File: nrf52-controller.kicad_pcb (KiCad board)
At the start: 8 copper layers, 32.3 x 27.6 mm, 94 parts, among them J1 Conn_01x01_Pin, J2 Conn_01x01_Pin, J3 USB_C_Receptacle_USB2.0, J4 Conn_01x01_Pin, J5 Conn_01x01_Pin, J6 Conn_ARM_JTAG_SWD_10, J7 FH35C-41S-0.3SHW, SW1 434351045816, SW2 434351045816, U1 MAX17048G+T10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

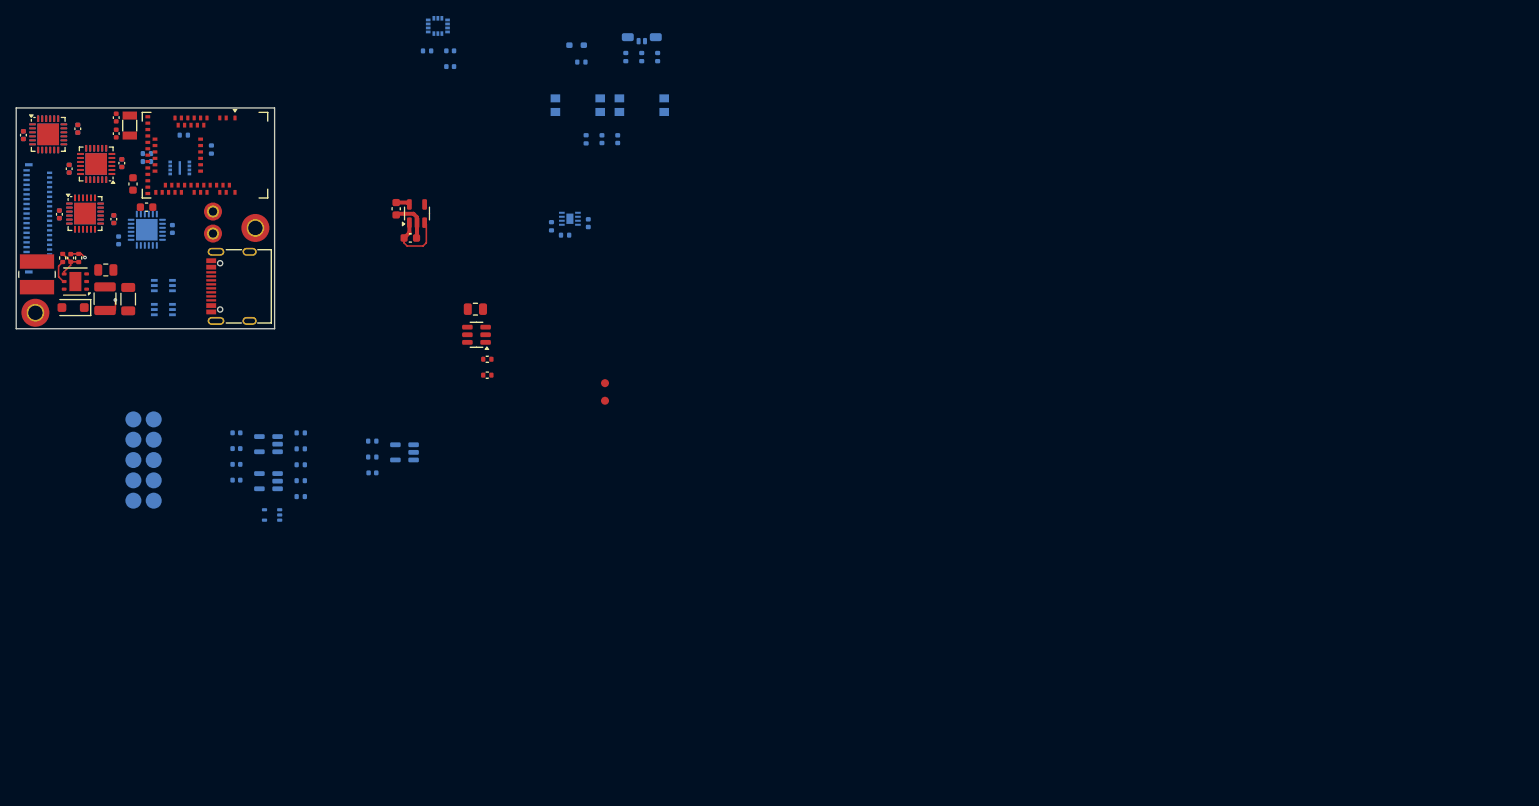
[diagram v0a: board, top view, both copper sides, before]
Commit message: separated smaller board layout variant
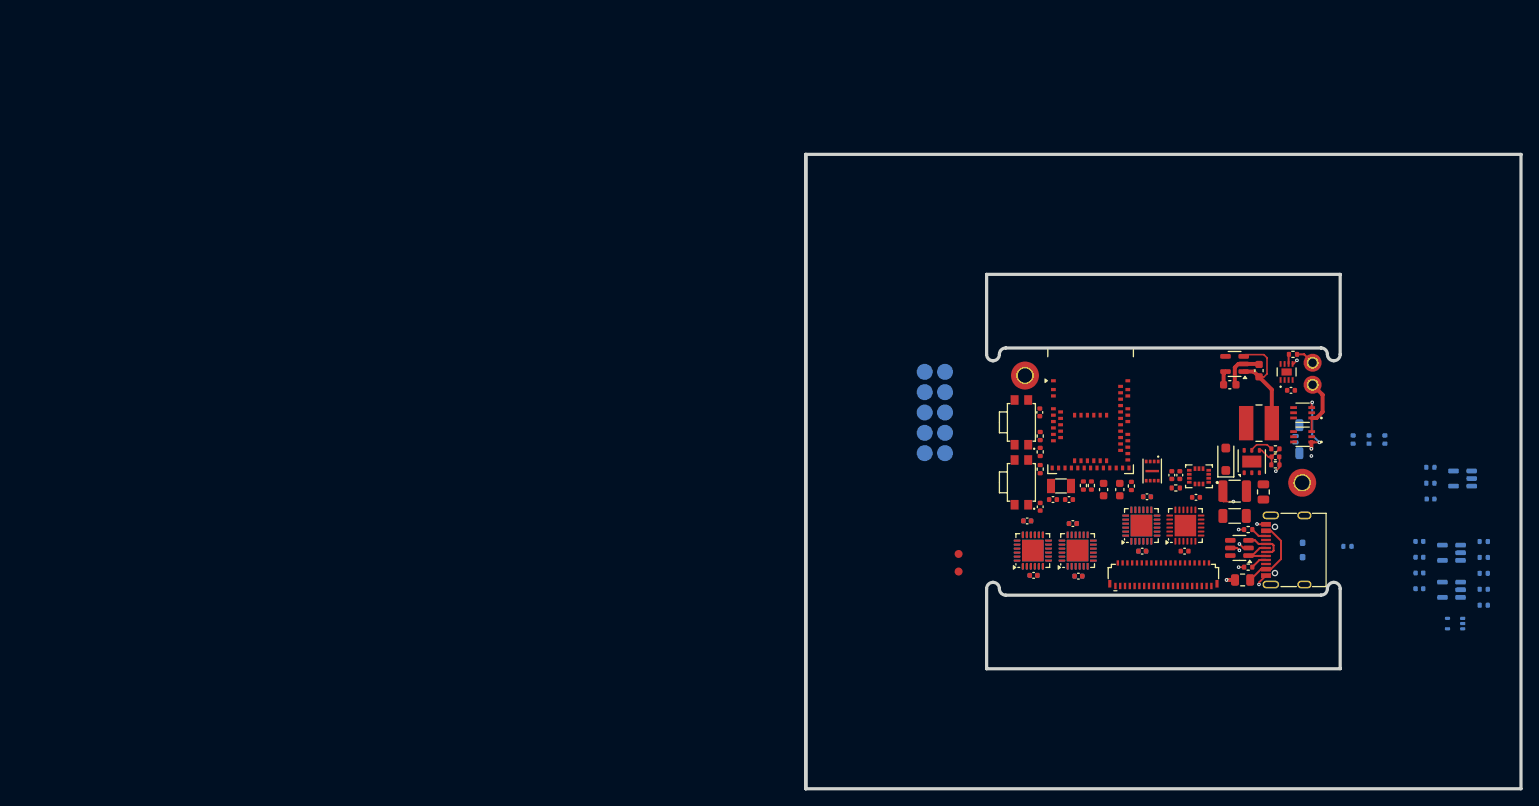
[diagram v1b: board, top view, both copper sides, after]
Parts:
- C1, C20, C24, C3, C33, C35, C4, HBD7, J7, R1, R11, R20, R21, R3, R7, R8, R9, SW1, SW2, U1, U13, U4, U6, U7: moved to F.Cu
- moved H1 159.8 mm to (195.3, 90.0)
- moved L1 153.9 mm to (189.9, 82.6), turned to 180 degrees
- moved R12 153.5 mm to (192.0, 85.8), turned to 180 degrees
- moved C5 152.6 mm to (192.0, 86.8), turned to 0 degrees
- moved R10 151.8 mm to (192.0, 87.8), turned to 180 degrees
- moved U5 148.8 mm to (189.1, 87.4), turned to 90 degrees
- moved C26 148.5 mm to (210.0, 97.4)
- moved C27 148.5 mm to (210.0, 99.4)
- moved C28 148.5 mm to (210.0, 101.3)
- moved C29 148.5 mm to (210.0, 103.3)
- moved R14 148.5 mm to (218.0, 97.4)
- moved R15 148.5 mm to (218.0, 99.4)
- moved R16 148.5 mm to (218.0, 101.4)
- moved R18 148.5 mm to (218.0, 103.4)
- moved R19 148.5 mm to (218.0, 105.4)
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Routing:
- net /Microcontroller/VBUS: track 0.00 -> 34.6 mm, vias 0 -> 6
- net /VBUS_IN: track 0.00 -> 9.61 mm
- net GND: track 8.46 -> 16.2 mm, vias 0 -> 5
- net /Power Selection and Regulation/VBAT: track 0.00 -> 7.29 mm
- net VIN: track 8.52 -> 15.0 mm
- net /D+_IN: track 0.00 -> 5.06 mm
- net /D-_IN: track 0.00 -> 4.79 mm
- net /CC1: track 0.00 -> 2.09 mm
- net /CC2: track 0.00 -> 2.05 mm
- net Net-(U1-QSTRT): track 0.00 -> 1.21 mm
- net ~{FG_ALERT}: track 0.00 -> 0.73 mm, vias 0 -> 1
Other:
- board size 32.3 x 27.6 mm -> 89.4 x 79.3 mm
